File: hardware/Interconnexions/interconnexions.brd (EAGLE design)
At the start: 248.9 x 81.3 mm, 102 parts, among them K5 ZNS5106

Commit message: 1 carte. 3 strap.
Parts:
- removed 24V_BATT: (no value), con-amp:1X2MTA
- removed C17, C18: (no value), resistor:E2,5-6E
- added AX12-7, AX12-8: (no value), con-amp:10X03MTA
- added BORNIER_LI-PO: (no value), con-ptr500:AK300/2
- ARRET_URGENCE, BORNIER_MONTE-PLOT, BORNIER_MOTEUR_DROIT, BORNIER_MOTEUR_GAUCHE, BUZZER, BYPASS_RELAI: device con-amp:1X2MTA -> con-ptr500:AK300/2
- D1, D2, D3, D4: value 1N4728 -> (none); device diode:DO41Z10 -> diode:ZDIO-2.5
- LED1: value (none) -> RED
- LED2: value (none) -> GREEN half
- LED3: value (none) -> GREEN full
- MD-PD-PWM, MG-PD-PWM, MP-PD-PWM: device rcl:0207/7 -> resistor:0207/7
- MD-PU-PWM, MG-PU-PWM, MP-PU-PWM: device rcl:0207/7 -> resistor:0207/15
- R3, R5, R6, R8: device resistor:0204/7 -> resistor:0207/2V
- moved R9 698.4 mm to (99.1, 16.5), turned to 180 degrees
- moved D5 675.2 mm to (68.6, 10.2), turned to 270 degrees
- moved LED3 667.2 mm to (87.6, 3.81)
- moved R7 662.7 mm to (99.1, 20.1)
- moved R8 658.7 mm to (97.8, 8.89), turned to 180 degrees
- moved LED2 658.2 mm to (80.0, 3.81)
- moved T4 656.9 mm to (101.6, 11.4), turned to 270 degrees
- moved BUZZER 655.1 mm to (44.5, 7.62)
- moved LED1 649.3 mm to (72.4, 3.81)
- moved D4 645.3 mm to (96.5, 12.7), turned to 270 degrees
- moved R6 645.0 mm to (88.9, 8.89), turned to 180 degrees
- moved T3 636.8 mm to (92.7, 11.4), turned to 270 degrees
- moved D3 632.4 mm to (87.6, 12.7), turned to 270 degrees
- moved R5 622.3 mm to (80.0, 8.89), turned to 180 degrees
- moved T2 620.4 mm to (83.8, 11.4), turned to 270 degrees
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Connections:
- removed net N$22: 24V_BATT.1, DIODE24V.A
- new net N$38: ARRET_URGENCE.2, DIODE24V.A
- net +24V_BATT: now also DIODE24V.C; no longer ARRET_URGENCE.1
- net +9V: now also AX12-7.2, AX12-8.2; no longer C17.+, C18.+
- net GND: now also AX12-7.1, AX12-8.1, BORNIER_LI-PO.1, BUZZER.2; no longer 24V_BATT.2, BUZZER.1, C17.-, C18.-
- net MONTE-PLOT_DIR: now also U$1.P$46; no longer U$1.P$42
- net MOTEUR_DROIT-DIR: now also U$1.P$44; no longer U$1.P$46
- net MOTEUR_DROIT-PWM: now also U$1.P$97; no longer U$1.P$98
- net MOTEUR_GAUCHE-DIR: now also U$1.P$42; no longer U$1.P$44
- net MOTEUR_GAUCHE-PWM: now also U$1.P$98; no longer U$1.P$97
- net N$23: now also ARRET_URGENCE.1, BORNIER_LI-PO.2; no longer ARRET_URGENCE.2, DIODE24V.C
- net N$28: now also BUZZER.1; no longer BUZZER.2
- net UART_AX12: now also AX12-7.3, AX12-8.3
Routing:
- net +9V: track 0.00 -> 548.3 mm
- net UART_AX12: track 0.00 -> 404.6 mm
- net +5V: track 0.00 -> 375.6 mm, vias 0 -> 2
- net +24V: track 0.00 -> 298.1 mm
- net MOTEUR_GAUCHE-DIR: track 0.00 -> 168.5 mm
- net MOTEUR_DROIT-DIR: track 0.00 -> 144.6 mm
- net MOTEUR_GAUCHE-PWM: track 0.00 -> 143.1 mm
- net N$28: track 0.00 -> 139.3 mm
- net MOTEUR_DROIT-PWM: track 0.00 -> 121.7 mm
- net MONTE-PLOT_DIR: track 0.00 -> 119.9 mm
- net MONTE-PLOT_PWM: track 0.00 -> 106.5 mm
- net UART_JAUNE: track 0.00 -> 78.5 mm
- net UART_ROUGE: track 0.00 -> 75.2 mm
- net +24V_BATT: track 0.00 -> 59.4 mm
- net CAPTEUR_A1: track 0.00 -> 39.7 mm
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- added copper zone on layer 16, net GND
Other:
- board size 248.9 x 81.3 mm -> 248.9 x 88.9 mm
- board text added: "ICI, BIENTÔT : Les circuits des DELs, et autres fioritures exquises qui font qu'on se souvient du robot !"
- board text added: "ICI, BIENTÔT : RIEN."

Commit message: Carte : modification de la distance interpistes
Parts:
- D5: value 1N4933 -> (none); device diode:DO41-10 -> diode:D-2.5
- MD-PD-DIR, MP-PD-DIR: device rcl:0207/7 -> rcl:0207/10
- R1: device resistor:0204/7 -> rcl:0207/2V
- R8: device resistor:0207/2V -> rcl:0204/5
- moved L2 33.3 mm to (80.0, 76.2), turned to 180 degrees
- moved C4 29.0 mm to (73.7, 67.3), turned to 270 degrees
- moved DC2 28.5 mm to (72.4, 76.2)
- moved RASPBERRY 24.5 mm to (83.8, 47.0), turned to 90 degrees
- moved C3 19.8 mm to (80.0, 67.3), turned to 0 degrees
- moved L3 12.0 mm to (77.5, 59.7)
- moved DC3 9.16 mm to (88.9, 57.1), turned to 0 degrees
- moved D5 3.81 mm to (68.6, 14.0)
- moved R8 3.42 mm to (96.5, 5.71), turned to 90 degrees
- moved C5 1.80 mm to (76.2, 50.8), turned to 0 degrees
- moved MD-PD-PWM 1.42 mm to (41.3, 30.5)
- moved R1 1.27 mm to (73.7, 16.5)
- moved C11 0.81 mm to (72.4, 42.0)
- turned R6 to 0 degrees
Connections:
- net CAPTEUR_4: now also U$1.P$88; no longer U$1.P$90
- net CAPTEUR_A1: now also U$1.P$18; no longer U$1.P$7
- net CAPTEUR_A2: now also U$1.P$16; no longer U$1.P$9
- net CODDROITB: now also U$1.P$75; no longer U$1.P$88
- net GND: now also U$1.P$24, U$1.P$65, U$1.P$66, U$1.P$91, U$1.P$92; no longer U$1.P$99
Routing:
- net +24V: track 298.1 -> 268.9 mm
- net CAPTEUR_A1: track 39.7 -> 61.9 mm
- net +15V: track 5.04 -> 22.7 mm
- net CAPTEUR_A2: track 34.6 -> 50.0 mm
- net N$28: track 139.3 -> 126.4 mm
- net CODDROITB: track 26.2 -> 16.4 mm, vias 2 -> 0
- net +9V: track 548.3 -> 540.1 mm
- net N$36: track 5.08 -> 0.00 mm
- net N$35: track 4.57 -> 0.00 mm
- net +24V_BATT: track 59.4 -> 63.8 mm
- net N$37: track 4.32 -> 0.00 mm
- net CAPTEUR_4: track 11.5 -> 15.5 mm
- net N$3: track 19.3 -> 15.6 mm
- net N$2: track 13.7 -> 11.3 mm
- net CODGAUCHEA: track 37.9 -> 35.9 mm, vias 2 -> 0
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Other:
- board size 248.9 x 88.9 mm -> 248.9 x 89.5 mm

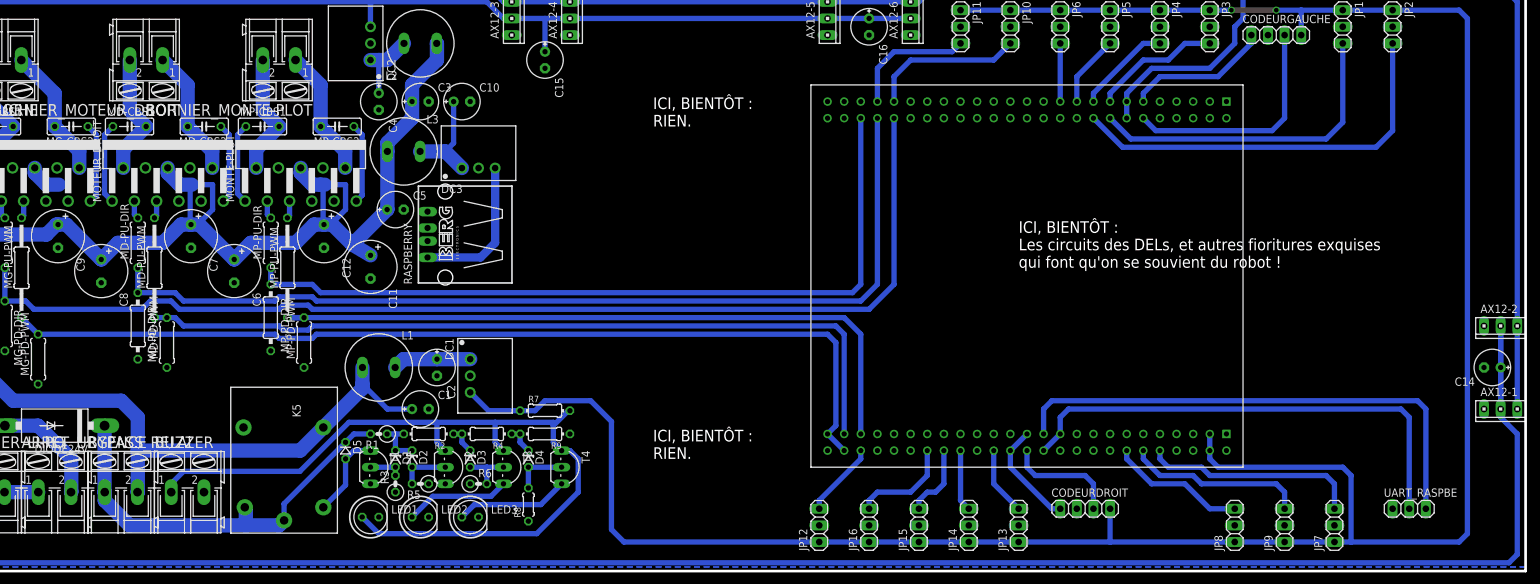
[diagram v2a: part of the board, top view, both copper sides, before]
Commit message: Carte d'interconnexions fonctionnelle
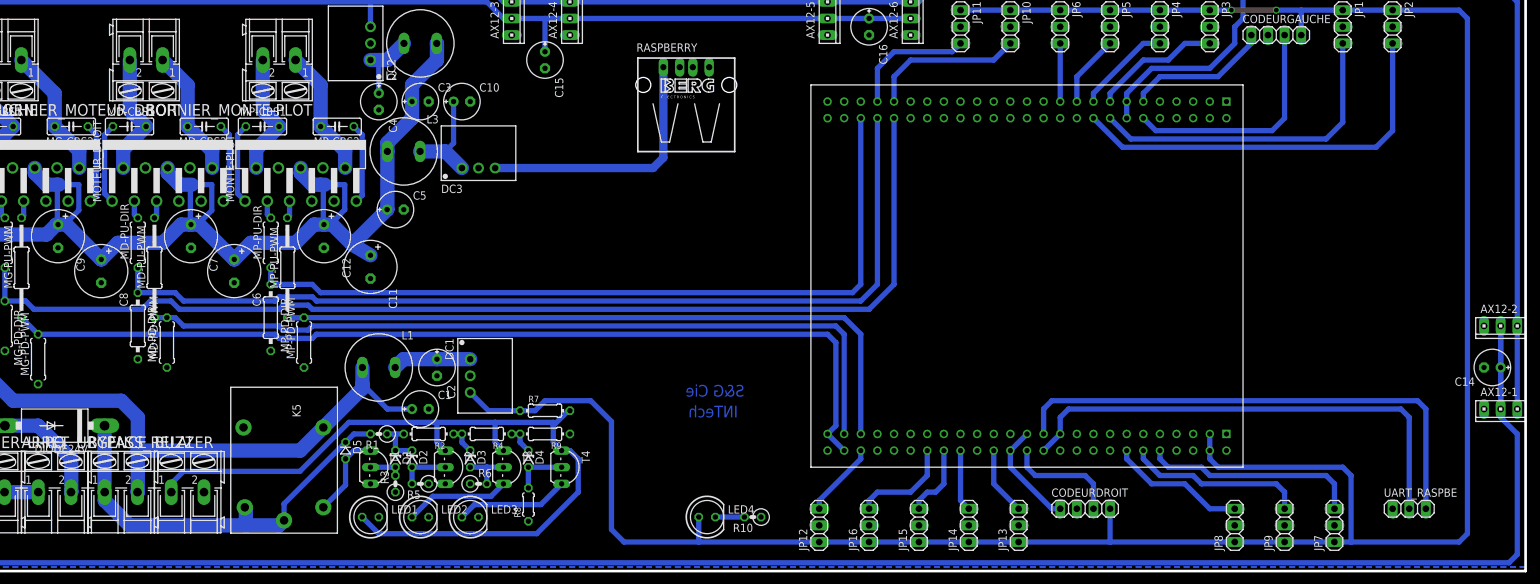
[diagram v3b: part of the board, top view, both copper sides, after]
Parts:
- added LED4: GREEN, led:LED5MM
- added R10: 1k, rcl:0207/2V
- moved RASPBERRY 43.3 mm to (120.7, 69.8), turned to 0 degrees
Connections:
- new net N$22: LED4.K, R10.2
- net +5V: now also LED4.A
- net GND: now also R10.1
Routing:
- net +15V: track 22.7 -> 40.2 mm
- net +24V: track 268.9 -> 284.7 mm
- net N$22: track 0.00 -> 4.44 mm
- net +5V: track 375.6 -> 379.4 mm
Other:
- board text added: "INTech"
- board text added: "S&G Cie"
- board text removed: "ICI, BIENTÔT : Les circuits des DELs, et autres fioritures exquises qui font qu'on se souvient du robot !"
- board text removed: "ICI, BIENTÔT : RIEN."

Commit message: documentation carte d'interconnexions
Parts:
- R10: value 1k -> 270
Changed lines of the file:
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@@
 <layer number="18" name="Vias" color="2" fill="1" visible="yes" active="yes"/>
 <layer number="19" name="Unrouted" color="6" fill="1" visible="yes" active="yes"/>
-<layer number="20" name="Dimension" color="15" fill="1" visible="no" active="yes"/>
-<layer number="21" name="tPlace" color="7" fill="1" visible="no" active="yes"/>
-<layer number="22" name="bPlace" color="7" fill="1" visible="no" active="yes"/>
-<layer number="23" name="tOrigins" color="15" fill="1" visible="no" active="yes"/>
+<layer number="20" name="Dimension" color="15" fill="1" visible="yes" active="yes"/>
+<layer number="21" name="tPlace" color="7" fill="1" visible="yes" active="yes"/>
+<layer number="22" name="bPlace" color="7" fill="1" visible="yes" active="yes"/>
+<layer number="23" name="tOrigins" color="15" fill="1" visible="yes" active="yes"/>
 <layer number="24" name="bOrigins" color="15" fill="1" visible="no" active="yes"/>
-<layer number="25" name="tNames" color="7" fill="1" visible="no" active="yes"/>
+<layer number="25" name="tNames" color="7" fill="1" visible="yes" active="yes"/>
 <layer number="26" name="bNames" color="7" fill="1" visible="no" active="yes"/>
 <layer number="27" name="tValues" color="7" fill="1" visible="no" active="yes"/>
@@
 <element name="AX12-7" library="con-amp" package="10X03MTA" value="" x="3.81" y="20.32"/>
 <element name="AX12-8" library="con-amp" package="10X03MTA" value="" x="3.81" y="33.02"/>
-<element name="R10" library="rcl" package="0207/2V" value="1k" x="130.81" y="3.81" rot="R180"/>
+<element name="R10" library="rcl" package="0207/2V" value="270" x="130.81" y="3.81" rot="R180"/>
 <element name="LED4" library="led" package="LED5MM" value="GREEN" x="123.825" y="3.81"/>
 </elements>

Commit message: maj doc cartes elec
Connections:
- net CAPTEUR_A1 renamed CAPTEUR_A1_US
- net CAPTEUR_A3 renamed CAPTEUR_A3_US
- net CAPTEUR_A4 renamed CAPTEUR_A4_US
- net CAPTEUR_A6 renamed CAPTEUR_A6_US
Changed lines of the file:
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@@
 <wire x1="140.97" y1="6.35" x2="140.97" y2="5.08" width="0.8128" layer="16"/>
 </signal>
-<signal name="CAPTEUR_A1">
+<signal name="CAPTEUR_A1_US">
 <contactref element="JP2" pad="3"/>
 <contactref element="U$1" pad="P$18"/>
@@
 <wire x1="220.98" y1="64.135" x2="220.98" y2="76.2" width="0.8128" layer="16"/>
 </signal>
-<signal name="CAPTEUR_A3">
+<signal name="CAPTEUR_A3_US">
 <contactref element="JP3" pad="3"/>
 <contactref element="U$1" pad="P$15"/>
@@
 <wire x1="180.34" y1="71.12" x2="185.42" y2="76.2" width="0.8128" layer="16"/>
 </signal>
-<signal name="CAPTEUR_A4">
+<signal name="CAPTEUR_A4_US">
 <contactref element="JP4" pad="3"/>
 <contactref element="U$1" pad="P$17"/>
@@
 <wire x1="190.5" y1="76.2" x2="193.04" y2="76.2" width="0.8128" layer="16"/>
 </signal>
-<signal name="CAPTEUR_A6">
+<signal name="CAPTEUR_A6_US">
 <contactref element="JP6" pad="3"/>
 <contactref element="U$1" pad="P$21"/>

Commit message: maj doc hardware
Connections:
- net CAPTEUR_A1_US renamed CAPTEUR_US_AV_D
- net CAPTEUR_A4_US renamed CAPTEUR_US_AR_D
- net CAPTEUR_A5 renamed CAPTEUR_A1
- net CAPTEUR_A6_US renamed CAPTEUR_US_AR_G
- removed net CAPTEUR_A3_US: JP3.3, U$1.P$15
- new net CAPTEUR_US_AV_G: JP1.3, U$1.P$16
- net CAPTEUR_1: now also JP16.3, U$1.P$88; no longer JP13.3, U$1.P$80
- net CAPTEUR_2: now also JP15.3, U$1.P$86; no longer JP14.3, U$1.P$84
- net CAPTEUR_3: now also JP14.3, U$1.P$84; no longer JP15.3, U$1.P$86
- net CAPTEUR_4: now also JP13.3, U$1.P$80; no longer JP16.3, U$1.P$88
- net CAPTEUR_A2: now also JP3.3, U$1.P$15; no longer JP1.3, U$1.P$16
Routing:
- net CAPTEUR_US_AV_G: track 0.00 -> 50.0 mm
- net CAPTEUR_A2: track 50.0 -> 19.7 mm
- net CAPTEUR_A3_US: track 19.7 -> 0.00 mm
- net CAPTEUR_4: track 15.5 -> 10.5 mm
- net CAPTEUR_1: track 10.5 -> 15.5 mm
- net CAPTEUR_3: track 11.2 -> 9.42 mm
- net CAPTEUR_2: track 9.42 -> 11.2 mm
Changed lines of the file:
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@@
 <wire x1="179.07" y1="20.32" x2="229.87" y2="20.32" width="0.8128" layer="16"/>
 </signal>
-<signal name="CAPTEUR_1">
+<signal name="CAPTEUR_4">
 <contactref element="JP13" pad="3"/>
 <contactref element="U$1" pad="P$80"/>
@@
 <wire x1="167.64" y1="8.89" x2="171.45" y2="5.08" width="0.8128" layer="16"/>
 </signal>
-<signal name="CAPTEUR_2">
+<signal name="CAPTEUR_3">
 <contactref element="JP14" pad="3"/>
 <contactref element="U$1" pad="P$84"/>
@@
 <wire x1="162.56" y1="6.35" x2="163.83" y2="5.08" width="0.8128" layer="16"/>
 </signal>
-<signal name="CAPTEUR_3">
+<signal name="CAPTEUR_2">
 <contactref element="JP15" pad="3"/>
 <contactref element="U$1" pad="P$86"/>
@@
 <wire x1="160.02" y1="8.89" x2="160.02" y2="13.97" width="0.8128" layer="16"/>
 </signal>
-<signal name="CAPTEUR_4">
+<signal name="CAPTEUR_1">
 <contactref element="JP16" pad="3"/>
 <wire x1="148.59" y1="5.08" x2="148.59" y2="6.35" width="0.8128" layer="16"/>
@@
 <wire x1="140.97" y1="6.35" x2="140.97" y2="5.08" width="0.8128" layer="16"/>
 </signal>
-<signal name="CAPTEUR_A1_US">
+<signal name="CAPTEUR_US_AV_D">
 <contactref element="JP2" pad="3"/>
 <contactref element="U$1" pad="P$18"/>
@@
 <wire x1="228.6" y1="62.865" x2="228.6" y2="76.2" width="0.8128" layer="16"/>
 </signal>
-<signal name="CAPTEUR_A2">
+<signal name="CAPTEUR_US_AV_G">
 <contactref element="JP1" pad="3"/>
 <contactref element="U$1" pad="P$16"/>
@@
 <wire x1="220.98" y1="64.135" x2="220.98" y2="76.2" width="0.8128" layer="16"/>
 </signal>
-<signal name="CAPTEUR_A3_US">
+<signal name="CAPTEUR_A2">
 <contactref element="JP3" pad="3"/>
 <contactref element="U$1" pad="P$15"/>
@@
 <wire x1="196.85" y1="76.2" x2="200.66" y2="76.2" width="0.8128" layer="16"/>
 </signal>
-<signal name="CAPTEUR_A5">
+<signal name="CAPTEUR_A1">
 <contactref element="JP5" pad="3"/>
 <contactref element="U$1" pad="P$19"/>
@@
 <wire x1="180.34" y1="71.12" x2="185.42" y2="76.2" width="0.8128" layer="16"/>
 </signal>
-<signal name="CAPTEUR_A4_US">
+<signal name="CAPTEUR_US_AR_D">
 <contactref element="JP4" pad="3"/>
 <contactref element="U$1" pad="P$17"/>
@@
 <wire x1="190.5" y1="76.2" x2="193.04" y2="76.2" width="0.8128" layer="16"/>
 </signal>
-<signal name="CAPTEUR_A6_US">
+<signal name="CAPTEUR_US_AR_G">
 <contactref element="JP6" pad="3"/>
 <contactref element="U$1" pad="P$21"/>
